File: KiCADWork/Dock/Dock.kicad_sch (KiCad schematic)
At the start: 15 parts, among them J1 Conn_01x10_Socket, J1 USB_C_Receptacle, P1 USB_C_Plug, P2 USB_C_Plug

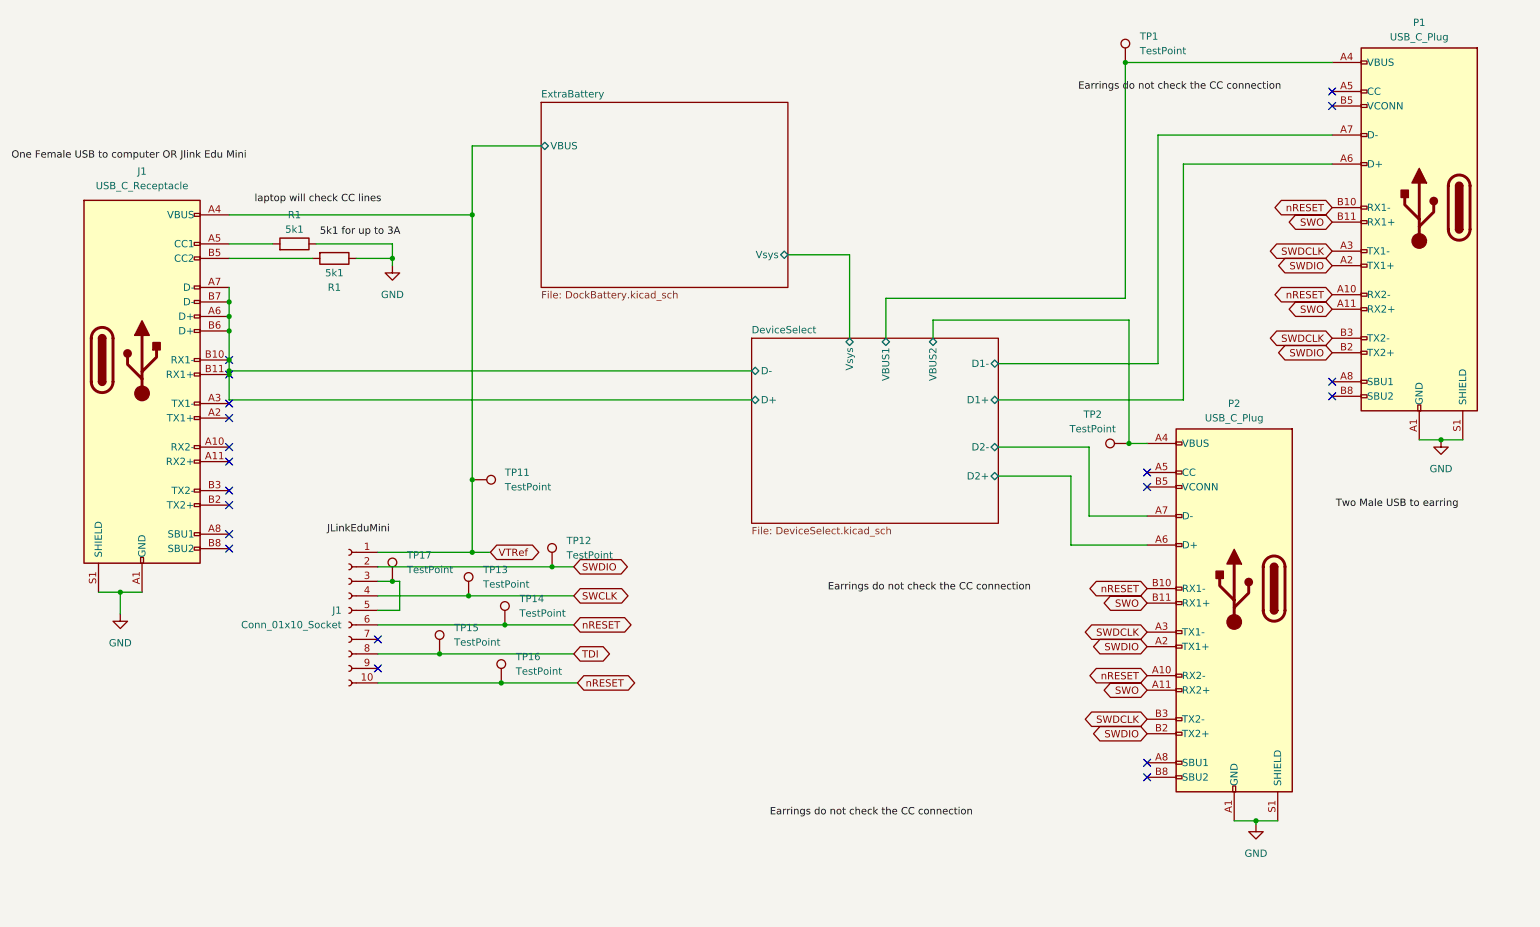
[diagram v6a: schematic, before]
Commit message: Dock Updates
Starting to layout the dock
Dom still to check
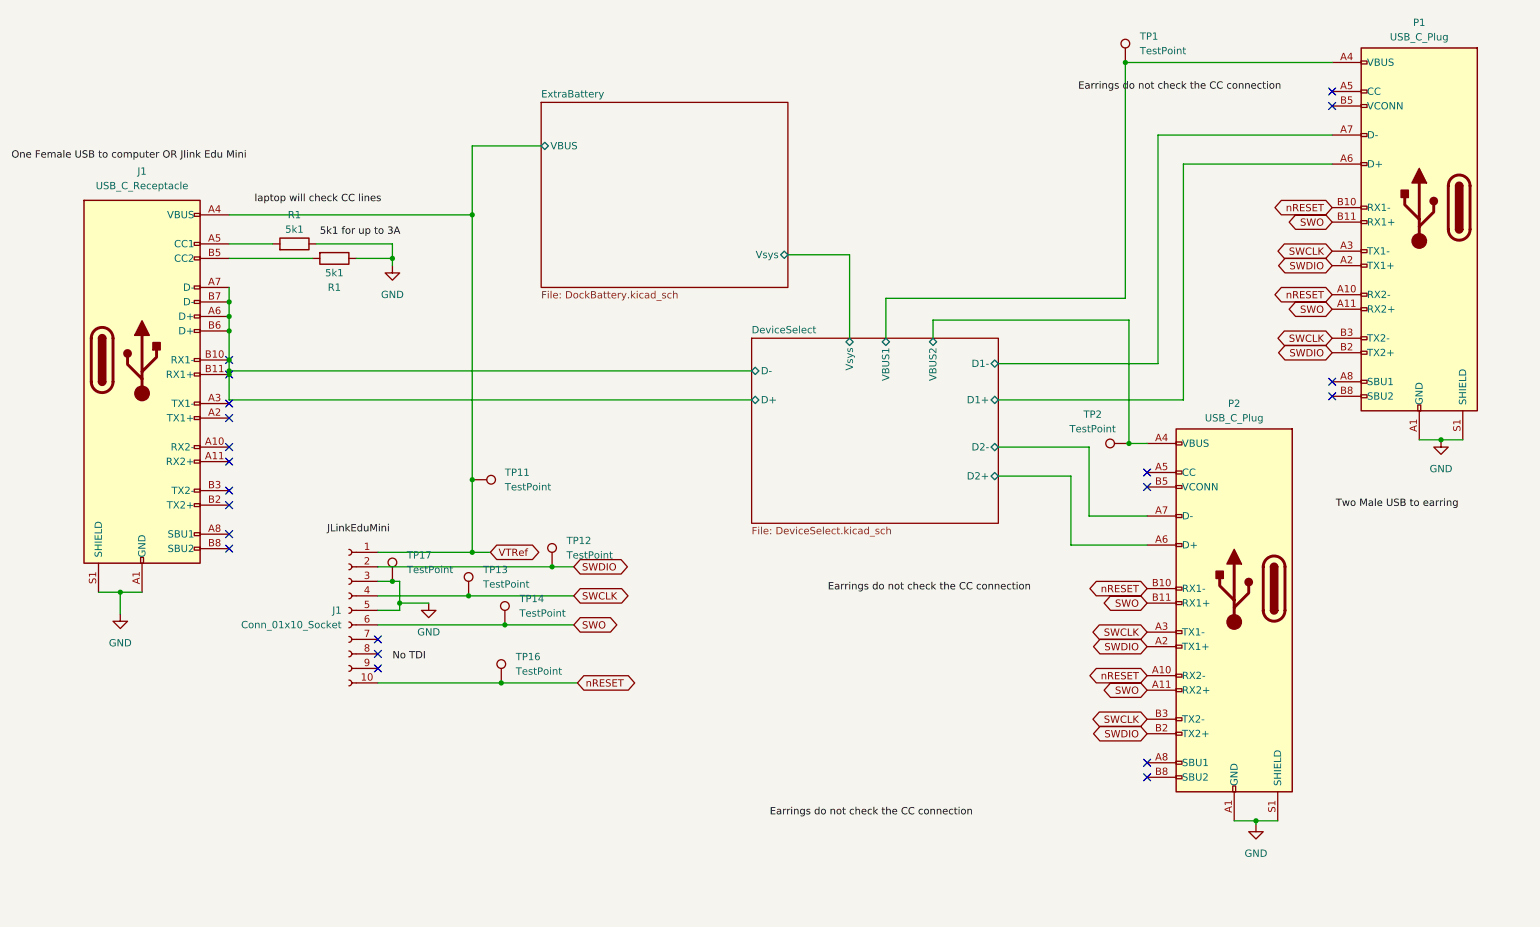
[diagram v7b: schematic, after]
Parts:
- removed TP15: TestPoint, TestPoint:TestPoint_Pad_D1.0mm, symbol Connector:TestPoint
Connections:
- net SWDCLK is gone; now on net SWCLK: P1.A3 (TX1-), P1.B3 (TX2-), P2.A3 (TX1-), P2.B3 (TX2-)
- net GND: now also J1.3 (Pin_3), J1.5 (Pin_5), TP17.1
- net SWO: now also J1.6 (Pin_6), TP14.1
- net nRESET: no longer J1.6 (Pin_6), TP14.1
- net TDI: no longer names the net of J1.8 (Pin_8)
- no-connect marks 20 -> 21
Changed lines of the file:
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@@
   (junction (at 57.15 63.5) (diameter 0) (color 0 0 0 0)
   )
-  (junction (at 93.98 125.095) (diameter 0) (color 0 0 0 0)
+  (junction (at 86.995 116.205) (diameter 0) (color 0 0 0 0)
   )
   (junction (at 104.775 130.175) (diameter 0) (color 0 0 0 0)
@@
   (no_connect (at 83.185 122.555))
   (no_connect (at 217.805 146.685))
+  (no_connect (at 83.185 125.095))
   (no_connect (at 250.19 29.21))
   (no_connect (at 83.185 127.635))
@@
     (stroke (width 0) (type default))
   )
-  (wire (pts (xy 93.98 125.095) (xy 83.185 125.095))
-    (stroke (width 0) (type default))
-  )
   (wire (pts (xy 83.185 130.175) (xy 104.775 130.175))
     (stroke (width 0) (type default))
@@
     (stroke (width 0) (type default))
   )
-  (wire (pts (xy 86.995 112.395) (xy 86.995 117.475))
+  (wire (pts (xy 86.995 112.395) (xy 86.995 116.205))
     (stroke (width 0) (type default))
   )
@@
     (stroke (width 0) (type default))
   )
-  (wire (pts (xy 117.475 125.095) (xy 93.98 125.095))
-    (stroke (width 0) (type default))
-  )
   (wire (pts (xy 236.855 154.305) (xy 240.665 154.305))
     (stroke (width 0) (type default))
@@
     (stroke (width 0) (type default))
   )
+  (wire (pts (xy 86.995 116.205) (xy 86.995 117.475))
+    (stroke (width 0) (type default))
+  )
   (wire (pts (xy 224.155 80.645) (xy 224.155 39.37))
     (stroke (width 0) (type default))
@@
     (stroke (width 0) (type default))
   )
+  (wire (pts (xy 92.075 116.205) (xy 86.995 116.205))
+    (stroke (width 0) (type default))
+  )
   (wire (pts (xy 83.185 112.395) (xy 85.725 112.395))
     (stroke (width 0) (type default))
@@
   )
   (label "One Female USB to computer OR Jlink Edu Mini" (at 19.05 38.735 0) (fields_autoplaced)
+    (effects (font (size 1.27 1.27)) (justify left bottom))
+  )
+  (label "No TDI" (at 85.725 126.365 0) (fields_autoplaced)
     (effects (font (size 1.27 1.27)) (justify left bottom))
   )
@@
     )
   )
-  (global_label "nRESET" (shape bidirectional) (at 117.475 120.015 0) (fields_autoplaced)
+  (global_label "SWO" (shape bidirectional) (at 117.475 120.015 0) (fields_autoplaced)
     (effects (font (size 1.27 1.27)) (justify left))
-    (property "Intersheetrefs" "${INTERSHEET_REFS}" (at 128.4656 120.015 0)
+    (property "Intersheetrefs" "${INTERSHEET_REFS}" (at 125.5629 120.015 0)
       (effects (font (size 1.27 1.27)) (justify left) hide)
     )
   )
-  (global_label "SWDCLK" (shape bidirectional) (at 217.805 121.285 180) (fields_autoplaced)
-    (effects (font (size 1.27 1.27)) (justify right))
-    (property "Intersheetrefs" "${INTERSHEET_REFS}" (at 206.2095 121.285 0)
-      (effects (font (size 1.27 1.27)) (justify right) hide)
-    )
-  )
-  (global_label "SWDCLK" (shape bidirectional) (at 250.19 69.85 180) (fields_autoplaced)
-    (effects (font (size 1.27 1.27)) (justify right))
-    (property "Intersheetrefs" "${INTERSHEET_REFS}" (at 238.5945 69.85 0)
+  (global_label "SWCLK" (shape bidirectional) (at 217.805 121.285 180) (fields_autoplaced)
+    (effects (font (size 1.27 1.27)) (justify right))
+    (property "Intersheetrefs" "${INTERSHEET_REFS}" (at 207.4795 121.285 0)
+      (effects (font (size 1.27 1.27)) (justify right) hide)
+    )
+  )
+  (global_label "SWCLK" (shape bidirectional) (at 250.19 69.85 180) (fields_autoplaced)
+    (effects (font (size 1.27 1.27)) (justify right))
+    (property "Intersheetrefs" "${INTERSHEET_REFS}" (at 239.8645 69.85 0)
       (effects (font (size 1.27 1.27)) (justify right) hide)
     )
@@
     )
   )
-  (global_label "SWDCLK" (shape bidirectional) (at 250.19 54.61 180) (fields_autoplaced)
-    (effects (font (size 1.27 1.27)) (justify right))
-    (property "Intersheetrefs" "${INTERSHEET_REFS}" (at 238.5945 54.61 0)
+  (global_label "SWCLK" (shape bidirectional) (at 250.19 54.61 180) (fields_autoplaced)
+    (effects (font (size 1.27 1.27)) (justify right))
+    (property "Intersheetrefs" "${INTERSHEET_REFS}" (at 239.8645 54.61 0)
       (effects (font (size 1.27 1.27)) (justify right) hide)
     )
@@
     )
   )
-  (global_label "SWDCLK" (shape bidirectional) (at 217.805 136.525 180) (fields_autoplaced)
-    (effects (font (size 1.27 1.27)) (justify right))
-    (property "Intersheetrefs" "${INTERSHEET_REFS}" (at 206.2095 136.525 0)
+  (global_label "SWCLK" (shape bidirectional) (at 217.805 136.525 180) (fields_autoplaced)
+    (effects (font (size 1.27 1.27)) (justify right))
+    (property "Intersheetrefs" "${INTERSHEET_REFS}" (at 207.4795 136.525 0)
       (effects (font (size 1.27 1.27)) (justify right) hide)
     )
@@
     (property "Intersheetrefs" "${INTERSHEET_REFS}" (at 242.1021 64.77 0)
       (effects (font (size 1.27 1.27)) (justify right) hide)
-    )
-  )
-  (global_label "TDI" (shape bidirectional) (at 117.475 125.095 0) (fields_autoplaced)
-    (effects (font (size 1.27 1.27)) (justify left))
-    (property "Intersheetrefs" "${INTERSHEET_REFS}" (at 124.4139 125.095 0)
-      (effects (font (size 1.27 1.27)) (justify left) hide)
     )
   )
@@
     (property "Intersheetrefs" "${INTERSHEET_REFS}" (at 209.7171 116.205 0)
       (effects (font (size 1.27 1.27)) (justify right) hide)
-    )
-  )
-  (symbol (lib_id "Connector:TestPoint") (at 93.98 125.095 0) (unit 1)
-    (in_bom yes) (on_board yes) (dnp no) (fields_autoplaced)
-    (property "Reference" "TP15" (at 96.52 120.523 0)
-      (effects (font (size 1.27 1.27)) (justify left))
-    )
-    (property "Value" "TestPoint" (at 96.52 123.063 0)
-      (effects (font (size 1.27 1.27)) (justify left))
-    )
-    (property "Footprint" "TestPoint:TestPoint_Pad_D1.0mm" (at 99.06 125.095 0)
-      (effects (font (size 1.27 1.27)) hide)
-    )
-    (property "Datasheet" "~" (at 99.06 125.095 0)
-      (effects (font (size 1.27 1.27)) hide)
-    )
-    (pin "1")
-    (instances
-      (project "Dock"
-        (path "/6f84fb5e-0715-49fa-a507-16643db39fa4"
-          (reference "TP15") (unit 1)
-        )
-      )
     )
   )
@@
         )
       )
+    )
+  )
+  (symbol (lib_id "power:GND") (at 92.075 116.205 0) (unit 1)
+    (in_bom yes) (on_board yes) (dnp no) (fields_autoplaced)
+    (property "Reference" "#PWR026" (at 92.075 122.555 0)
+      (effects (font (size 1.27 1.27)) hide)
+    )
+    (property "Value" "GND" (at 92.075 121.285 0)
+      (effects (font (size 1.27 1.27)))
+    )
+    (property "Footprint" "" (at 92.075 116.205 0)
+      (effects (font (size 1.27 1.27)) hide)
+    )
+    (property "Datasheet" "" (at 92.075 116.205 0)
+      (effects (font (size 1.27 1.27)) hide)
+    )
+    (pin "1")
+    (instances
+      (project "Dock"
+        (path "/6f84fb5e-0715-49fa-a507-16643db39fa4"
+          (reference "#PWR026") (unit 1)
+        )
+      )

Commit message: Initial Dock DRC Complete
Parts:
- removed TP1, TP2: TestPoint, TestPoint:TestPoint_Pad_D1.0mm, symbol Connector:TestPoint
- added C3 (x2): 100n, Capacitor_SMD:C_0402_1005Metric_Pad0.74x0.62mm_HandSolder, symbol Device:C
- added R1 (x2): 0R, Resistor_SMD:R_0805_2012Metric_Pad1.20x1.40mm_HandSolder, symbol Device:R
- added R11 (x2): 1k, Resistor_SMD:R_0402_1005Metric_Pad0.72x0.64mm_HandSolder, symbol Device:R
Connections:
- net DeviceSelect/D+: now also R1.1; no longer J1.A6 (D+), J1.A7 (D-), J1.B10 (RX1-), J1.B11 (RX1+), J1.B6 (D+), J1.B7 (D-)
- net GND: now also C3.1, C3.1, R11.2, R11.2; no longer P1.S1 (SHIELD), P2.S1 (SHIELD)
- new net: C3.2, P2.S1 (SHIELD), R11.1
- new net: J1.A6 (D+), J1.B6 (D+), R1.2
- new net: C3.2, P1.S1 (SHIELD), R11.1
- new net: J1.A7 (D-), J1.B7 (D-), R1.1
- new net DeviceSelect/D-: R1.2
